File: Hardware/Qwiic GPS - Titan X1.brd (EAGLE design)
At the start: 30.5 x 25.4 mm, 38 parts, among them J1 U.FL, J2 Qwiic Right Angle, J3 PTH, J4 Qwiic Right Angle, U1 Titan X1 GPS

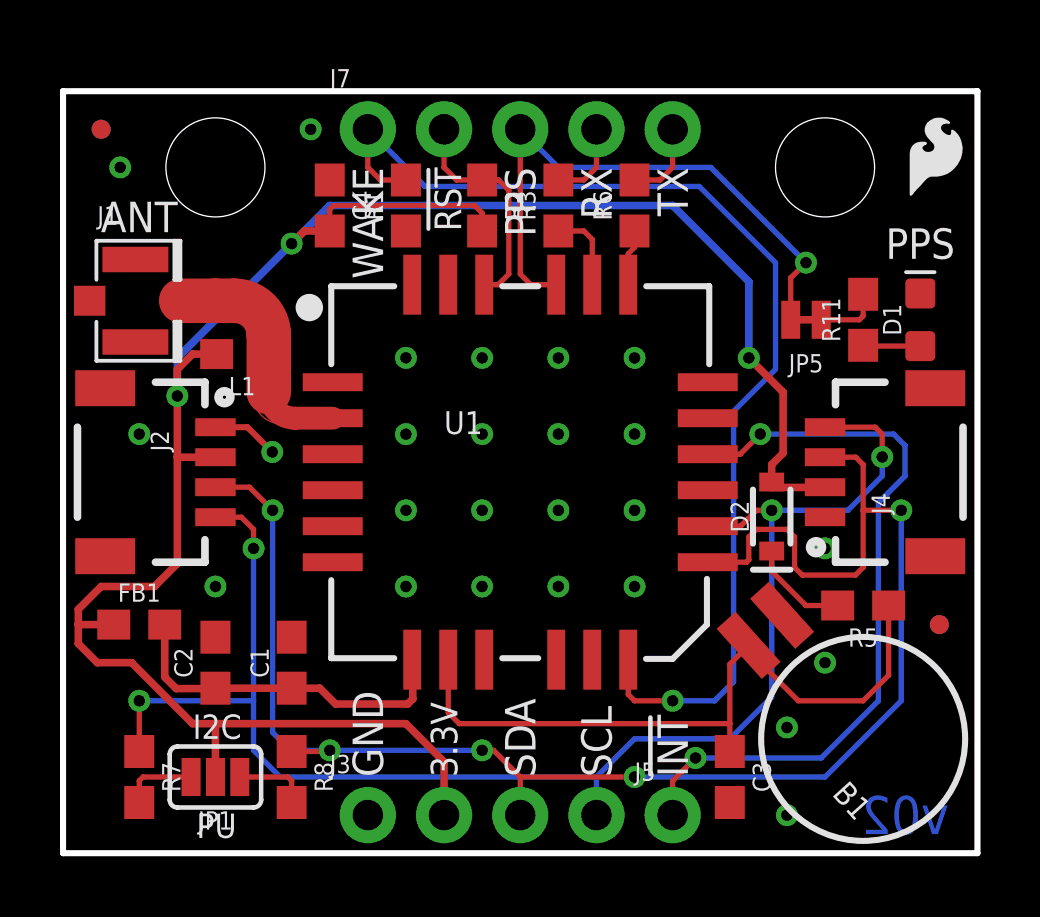
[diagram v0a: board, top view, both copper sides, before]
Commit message: Changed version number, moved int pin to be compatible with arduino, added jumper label for pps led
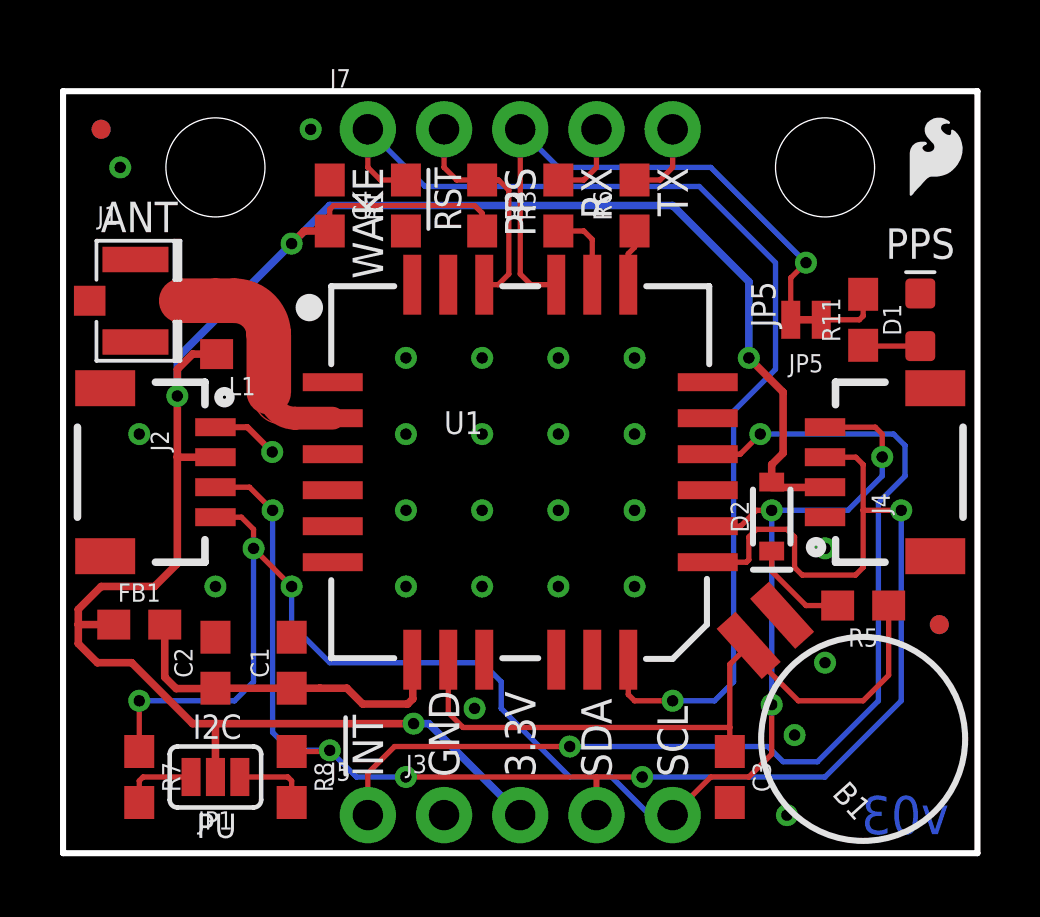
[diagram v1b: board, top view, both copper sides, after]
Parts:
- moved J5 10.2 mm to (10.2, 1.27)
- moved J3 2.54 mm to (12.7, 1.27)
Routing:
- net INT: track 25.0 -> 35.7 mm
- net SCL: track 50.4 -> 53.4 mm, vias 4 -> 6
- net 3.3V: track 73.7 -> 75.2 mm, vias 3 -> 4
- net GND: vias 25 -> 26
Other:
- board text added: "JP5"
- board text added: "v03"
- board text removed: "v02"
